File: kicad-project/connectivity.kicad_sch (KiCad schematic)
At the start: 7 parts

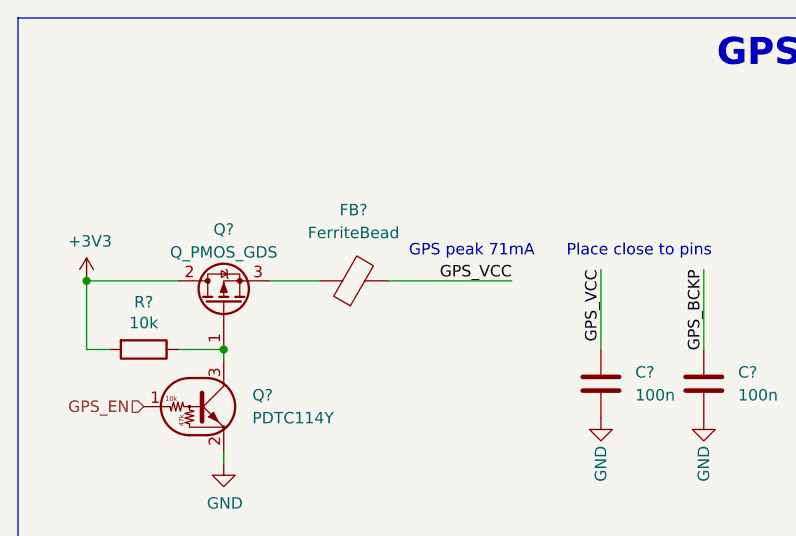
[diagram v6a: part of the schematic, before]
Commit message: hw: set grid to 50 mils and missing labels
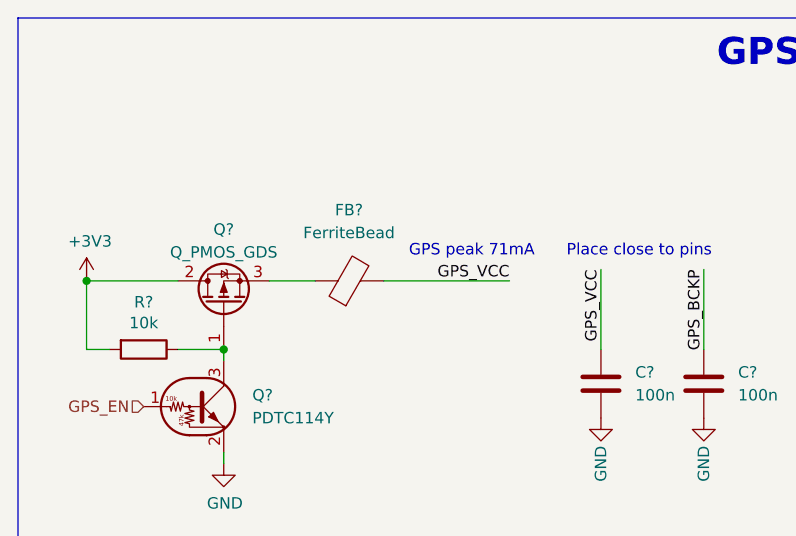
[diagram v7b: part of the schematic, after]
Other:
- moved on the sheet: FB?
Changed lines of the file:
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@@
     (stroke (width 0) (type default) (color 0 0 0 0))
   )
-  (wire (pts (xy 138.43 43.18) (xy 144.018 43.18))
+  (wire (pts (xy 138.43 43.18) (xy 143.51 43.18))
     (stroke (width 0) (type default) (color 0 0 0 0))
   )
-  (wire (pts (xy 151.638 43.18) (xy 165.354 43.18))
+  (wire (pts (xy 151.13 43.18) (xy 165.1 43.18))
     (stroke (width 0) (type default) (color 0 0 0 0))
   )
@@
     (effects (font (size 1.27 1.27)) (justify right bottom))
   )
-  (label "GPS_VCC" (at 165.354 43.18 180)
+  (label "GPS_VCC" (at 165.1 43.18 180)
     (effects (font (size 1.27 1.27)) (justify right bottom))
   )
@@
     (pin "1")
   )
-  (symbol (lib_id "Device:FerriteBead") (at 147.828 43.18 90) (unit 1)
+  (symbol (lib_id "Device:FerriteBead") (at 147.32 43.18 90) (unit 1)
     (in_bom yes) (on_board yes) (fields_autoplaced)
-    (property "Reference" "FB?" (id 0) (at 147.7772 35.306 90))
-    (property "Value" "FerriteBead" (id 1) (at 147.7772 37.846 90))
-    (property "Footprint" "" (id 2) (at 147.828 44.958 90)
+    (property "Reference" "FB?" (id 0) (at 147.2692 35.306 90))
+    (property "Value" "FerriteBead" (id 1) (at 147.2692 37.846 90))
+    (property "Footprint" "" (id 2) (at 147.32 44.958 90)
       (effects (font (size 1.27 1.27)) hide)
     )
-    (property "Datasheet" "~" (id 3) (at 147.828 43.18 0)
+    (property "Datasheet" "~" (id 3) (at 147.32 43.18 0)
       (effects (font (size 1.27 1.27)) hide)
     )

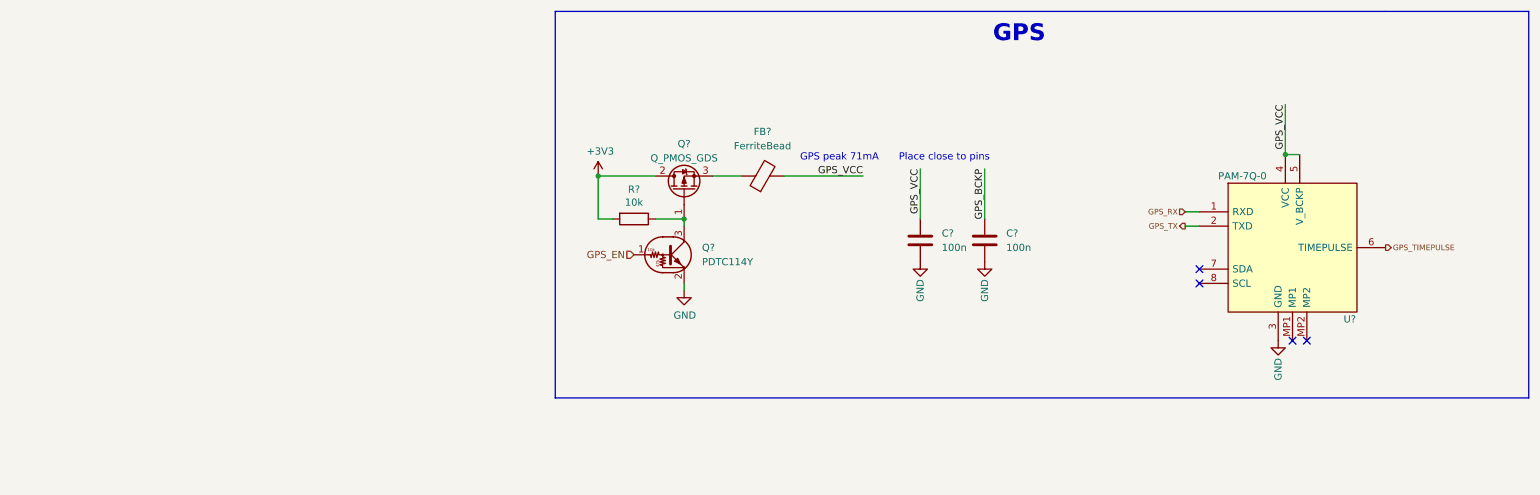
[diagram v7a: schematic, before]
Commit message: hw: add capacitor voltages, fix supply caps and other fixes
add capacitor voltages, change polarized caps to normal, move switching capacitors, remove 5V power, fix switching ballast capacitor, remove switching feedback capacitor, switch sensing and actuation sub-sheets positions in main sheet, add labels to most nodes for pcb layout, connect GPS supply caps directly, remove biased transistor and ferrite bead from GPS enable MOSFET, remove unneeded pins from stepper motors connectors
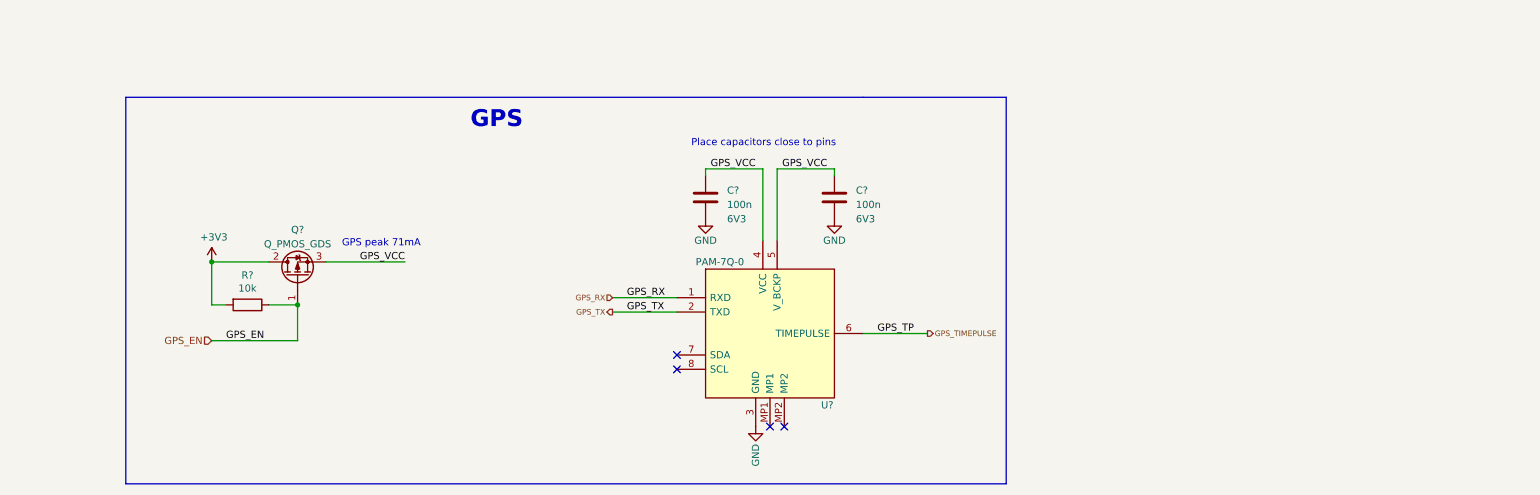
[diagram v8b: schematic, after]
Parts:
- removed C? (x2): 100n, symbol Device:C
- removed FB?: FerriteBead, symbol Device:FerriteBead
- removed Q?: PDTC114Y, symbol Transistor_BJT:DTC114Y
- added C? (x2): 100n, symbol Device:C
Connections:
- net GND: now also C?.2, C?.2
- net GPS_EN: now also Q?.1 (G), R?.1
- net GPS_VCC: now also Q?.3 (S), C?.1, C?.1
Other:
- note added: "Place capacitors close to pins"
- note removed: "Place close to pins"
- moved on the sheet: Q?, R?, U?
